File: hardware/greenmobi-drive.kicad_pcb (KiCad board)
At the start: 2 copper layers, 100 x 100 mm, 136 parts, among them J1 Sensors, J2 GND, J3 UBAT, J4 USB_C_Receptacle_USB2.0_14P, J5 CAN, J6 Debug, J7 Phase_OUT, J8 Phase_OUT, J9 Phase_OUT, Q11 AGM015N10LL, Q12 AGM015N10LL, Q17 AGM015N10LL, Q18 AGM015N10LL, Q2 MMBT3904, Q3 MMBT3904, Q5 AGM015N10LL, Q6 AGM015N10LL, SW1 BOOT, SW2 RESET, U1 TJA1051T-3, U10 AMS1117-3.3, U11 BMI323, U2 STM32F405RGTx, U3 IRS21867S, U4 INA240A2D, U5 IRS21867S, U6 INA240A2D, U7 IRS21867S, U8 INA240A2D, U9 LM5163DDA, Y1 8MHz

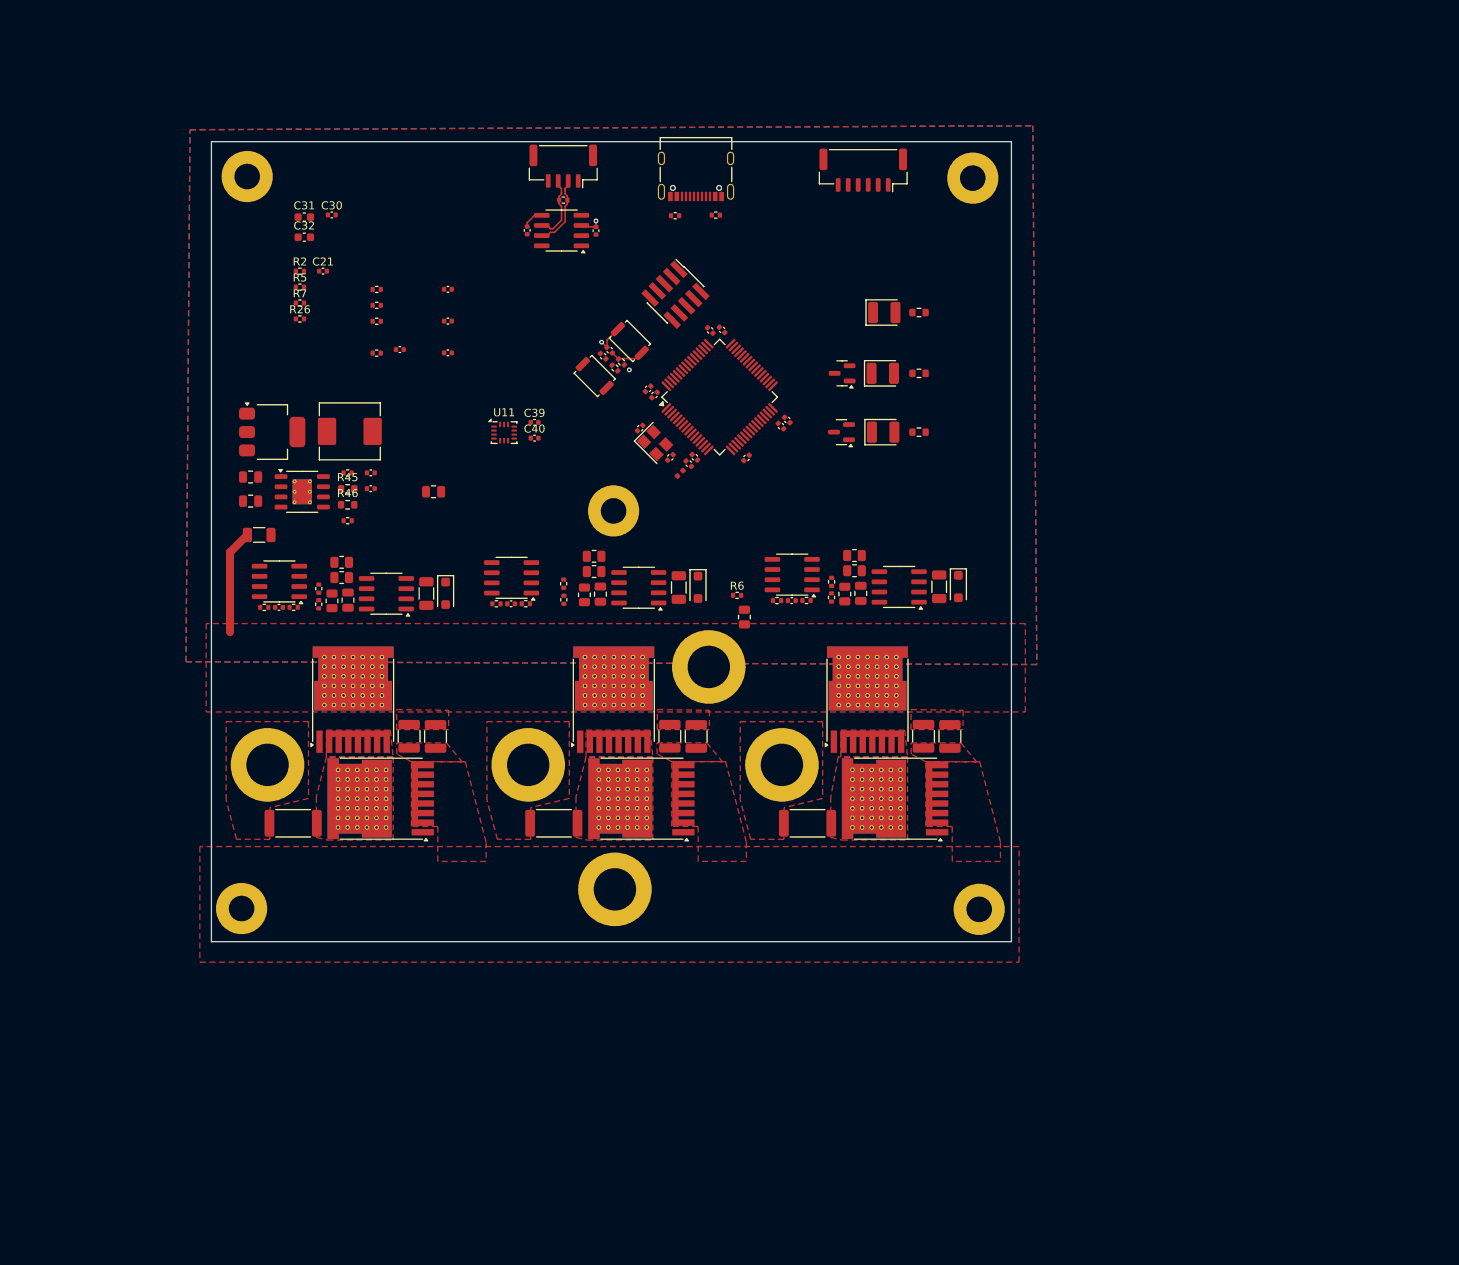
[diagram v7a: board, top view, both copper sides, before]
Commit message: Regulators layout
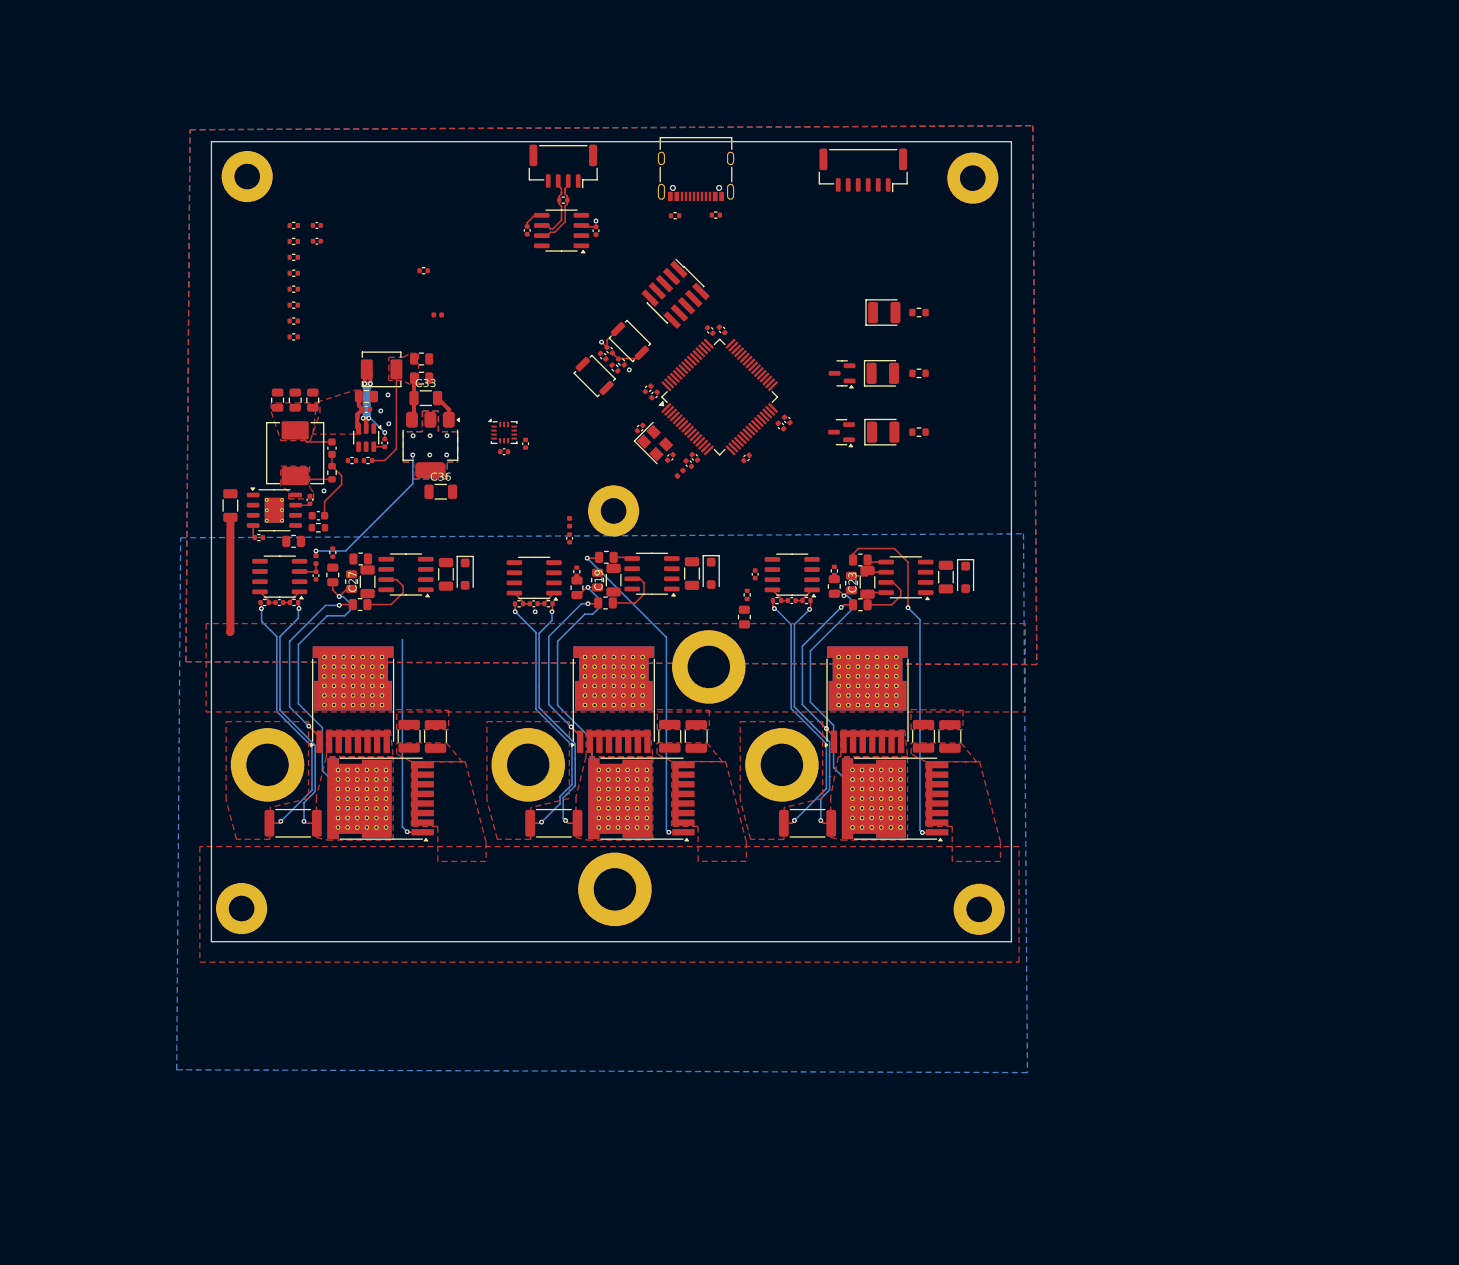
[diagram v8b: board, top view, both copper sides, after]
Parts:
- removed R47: 49.9, Resistor_SMD:R_0402_1005Metric
- added C41: 4.7u, Capacitor_SMD:C_0805_2012Metric, F.Cu at (113.3, 77.9)
- added C42: 100n, Capacitor_SMD:C_0402_1005Metric, F.Cu at (113.3, 79.5)
- added C43: 100n, Capacitor_SMD:C_0402_1005Metric, F.Cu at (115.6, 83.7)
- added C47: 22u, Capacitor_SMD:C_0805_2012Metric, F.Cu at (120.2, 73.2)
- added C48: 22u, Capacitor_SMD:C_0805_2012Metric, F.Cu at (120.2, 75.6)
- added L3: 15u, Inductor_SMD:L_Chilisin_BMRA00040420, F.Cu at (115.2, 74.5)
- added L4: L_Ferrite, Inductor_SMD:L_0402_1005Metric, F.Cu at (138.7, 93.6)
- added L5: L_Ferrite, Inductor_SMD:L_0402_1005Metric, F.Cu at (122.2, 67.7)
- added L6: L_Ferrite, Inductor_SMD:L_0402_1005Metric, F.Cu at (107.0, 98.3)
- added R10: 100k, Resistor_SMD:R_0402_1005Metric, F.Cu at (113.5, 85.9)
- added R48: 13.3k, Resistor_SMD:R_0402_1005Metric, F.Cu at (111.5, 85.9)
- added R49: 56k, Resistor_SMD:R_0805_2012Metric, F.Cu at (104.2, 96.0)
- added R9: 453k, Resistor_SMD:R_0402_1005Metric, F.Cu at (120.5, 62.2)
- added U12: TPS54202DDC, Package_TO_SOT_SMD:SOT-23-6, F.Cu at (113.3, 83.0)
- C19, C23, C27: footprint Capacitor_SMD:C_0805_2012Metric -> Capacitor_SMD:C_1206_3216Metric
- C33, C36: footprint Capacitor_SMD:C_0402_1005Metric -> Capacitor_SMD:C_1206_3216Metric
- R20, R29, R38: footprint Resistor_SMD:R_0402_1005Metric -> Resistor_SMD:R_0805_2012Metric
- R46: value 453k -> 511k
- moved C25 49.8 mm to (161.9, 100.1), turned to -90 degrees
- moved C38 39.4 mm to (107.0, 100.3), turned to -90 degrees
- moved C31 37.4 mm to (107.3, 92.8), turned to 180 degrees
- moved C30 35.7 mm to (106.2, 90.8), turned to 90 degrees
- moved C17 27.7 mm to (138.7, 95.6), turned to -90 degrees
- moved C32 26.6 mm to (109.0, 84.3), turned to 90 degrees
- moved C37 20.7 mm to (104.4, 78.4), turned to 90 degrees
- moved U10 19.8 mm to (121.3, 84.0), turned to -90 degrees
- moved C1 18.7 mm to (107.1, 56.5)
- moved C35 14.8 mm to (106.6, 78.4), turned to 90 degrees
- moved R44 13.7 mm to (99.9, 95.5)
- moved R1 13.1 mm to (104.2, 56.5)
- moved R4 12.0 mm to (104.2, 60.5)
- moved C33 11.6 mm to (120.7, 78.1)
- moved R8 10.6 mm to (104.2, 66.5)
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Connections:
- C17 pad 1: +3.3V -> Net-(U4-REF2)
- C25 pad 1: +3.3V -> Net-(U6-REF2)
- C38 pad 1: +3.3V -> Net-(U8-REF2)
- U4 pad 3: +3.3V -> Net-(U4-REF2)
- U4 pad 6: +3.3V -> Net-(U4-REF2)
- U6 pad 3: +3.3V -> Net-(U6-REF2)
- U6 pad 6: +3.3V -> Net-(U6-REF2)
- U8 pad 3: +3.3V -> Net-(U8-REF2)
- U8 pad 6: +3.3V -> Net-(U8-REF2)
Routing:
- net /half-bridge2/Center: track 0.00 -> 69.4 mm, vias 0 -> 3
- net /half-bridge/Center: track 0.00 -> 67.4 mm, vias 0 -> 3
- net /half-bridge1/Center: track 0.00 -> 65.7 mm, vias 0 -> 3
- net Net-(Q12-G): track 0.00 -> 45.0 mm, vias 0 -> 2
- net Net-(Q6-G): track 0.00 -> 41.8 mm, vias 0 -> 2
- net Net-(J8-Pin_1): track 0.00 -> 33.4 mm, vias 0 -> 2
- net Net-(J7-Pin_1): track 0.00 -> 33.3 mm, vias 0 -> 2
- net Net-(J9-Pin_1): track 0.00 -> 33.1 mm, vias 0 -> 2
- net Net-(Q18-G): track 0.00 -> 26.2 mm, vias 0 -> 1
- net Net-(Q17-G): track 0.00 -> 23.9 mm, vias 0 -> 2
- net Net-(Q5-G): track 0.00 -> 22.7 mm, vias 0 -> 2
- net Net-(Q11-G): track 0.00 -> 22.0 mm, vias 0 -> 2
- net Net-(U12-SW): track 0.00 -> 19.8 mm, vias 0 -> 5
- net +3.3V: track 6.49 -> 26.3 mm, vias 1 -> 8
- net +5V: track 2.64 -> 21.5 mm
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- added copper zone on F.Cu, net +12V
- added copper zone on B.Cu, net +3.3V
- added copper zone on F.Cu, net +3.3V
- added copper zone on F.Cu, net +5V
- added copper zone on F.Cu, net Net-(J7-Pin_1)
- added copper zone on F.Cu, net Net-(J9-Pin_1)
- added copper zone on F.Cu, net Net-(U9-SW)
